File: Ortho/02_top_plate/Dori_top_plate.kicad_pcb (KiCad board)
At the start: 2 copper layers, 307.2 x 111.1 mm, 84 parts, among them J1 4PIN, J2 4PIN, U1 HOLE, U10 HOLE, U11 HOLE, U12 HOLE, U13 HOLE, U14 HOLE, U15 HOLE, U16 HOLE, U17 HOLE, U18 HOLE, U19 HOLE, U2 HOLE, U20 HOLE, U21 HOLE, U22 HOLE, U23 HOLE, U24 HOLE, U25 HOLE, U26 HOLE, U27 HOLE, U28 HOLE, U29 HOLE, U3 HOLE, U30 HOLE, U31 HOLE, U32 HOLE, U33 HOLE, U34 HOLE, U35 HOLE, U36 HOLE, U37 HOLE, U38 HOLE, U39 HOLE, U4 HOLE, U40 HOLE, U41 HOLE, U42 HOLE, U43 HOLE, U44 HOLE, U45 HOLE, U46 HOLE, U47 HOLE, U48 HOLE, U49 HOLE, U5 HOLE, U50 HOLE, U51 HOLE, U52 HOLE, U53 HOLE, U54 HOLE, U55 HOLE, U56 HOLE, U57 HOLE, U58 HOLE, U59 HOLE, U6 HOLE, U60 HOLE, U61 HOLE, U62 HOLE, U63 HOLE, U64 HOLE, U65 HOLE, U66 HOLE, U67 HOLE, U68 HOLE, U7 HOLE, U8 HOLE, U9 HOLE

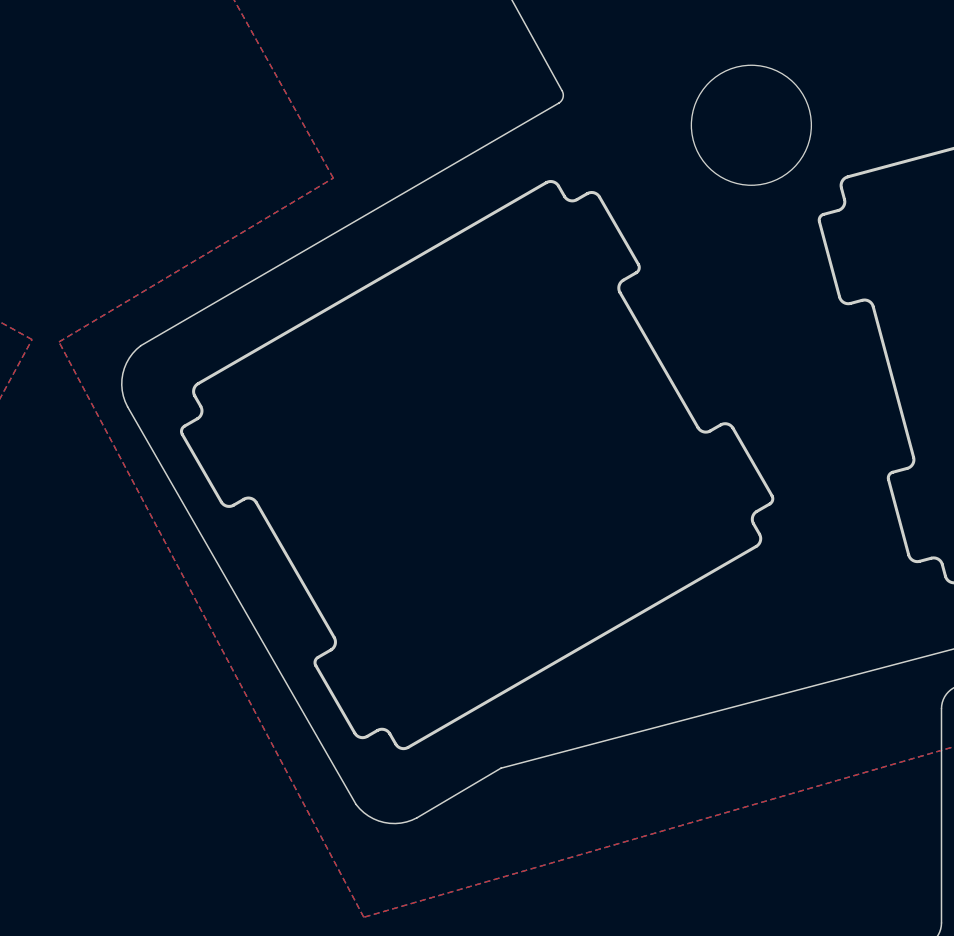
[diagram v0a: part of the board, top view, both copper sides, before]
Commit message: Moved USB port
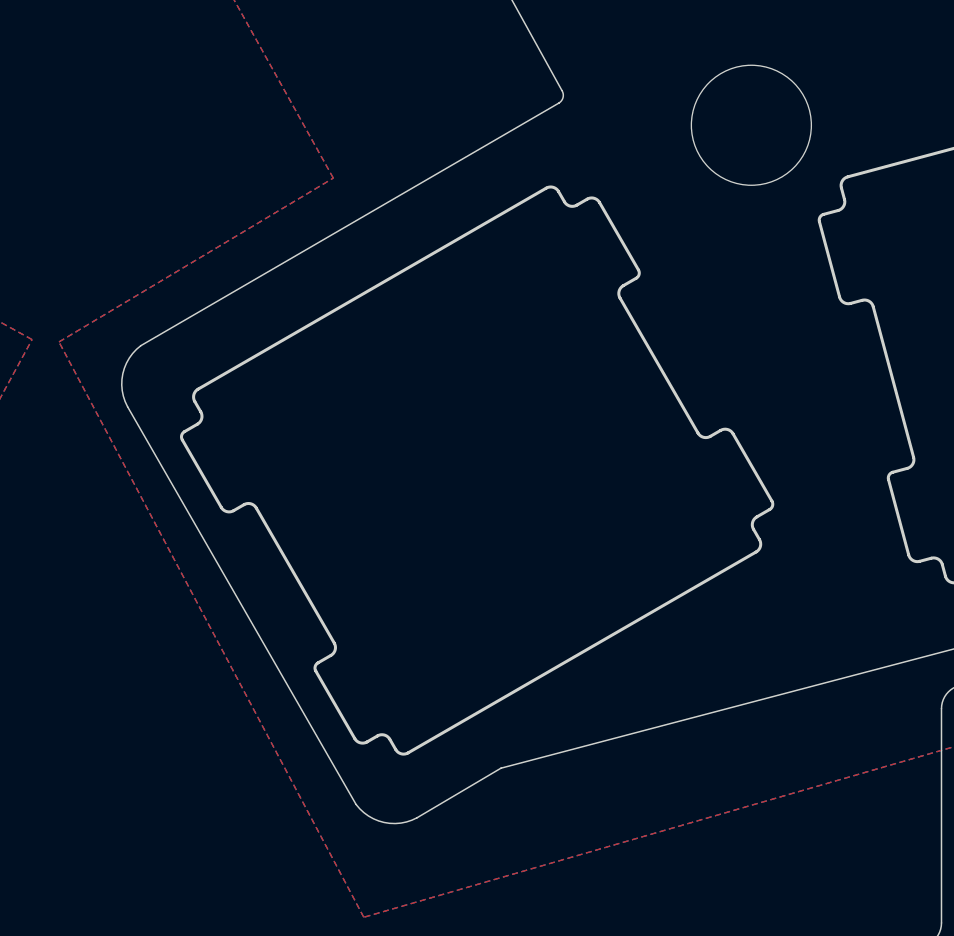
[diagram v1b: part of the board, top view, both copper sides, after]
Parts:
- moved U50 0.18 mm to (259.6, 116.7)
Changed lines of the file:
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@@
-(kicad_pcb (version 20171130) (host pcbnew "(5.1.2-1)-1")
+(kicad_pcb (version 20171130) (host pcbnew "(5.1.4-0-10_14)")
   (general
     (thickness 1.6)
@@
   )
   (module Keeb_footprints:MX100_slot (layer F.Cu)
-    (at 259.55625 116.498801 30)
+    (at 259.55625 116.68125 30)
     (fp_text reference U50 (at 0.0127 1.8288 30) (layer Dwgs.User)
       (effects (font (size 1 1) (thickness 0.15)))
